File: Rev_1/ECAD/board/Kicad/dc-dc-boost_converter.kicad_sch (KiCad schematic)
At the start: 90 parts, among them Q1 NPN, Q100 IPP029N15NM6, Q101 NPN, Q102 NPN, Q103 PMOS, SW1 SW_DIP_x04, U100 LM3478MA, U2 LM358, U3 LM358, U4 SN74AHC1G02DBVR, U5 SN74AHC1G02DBVR

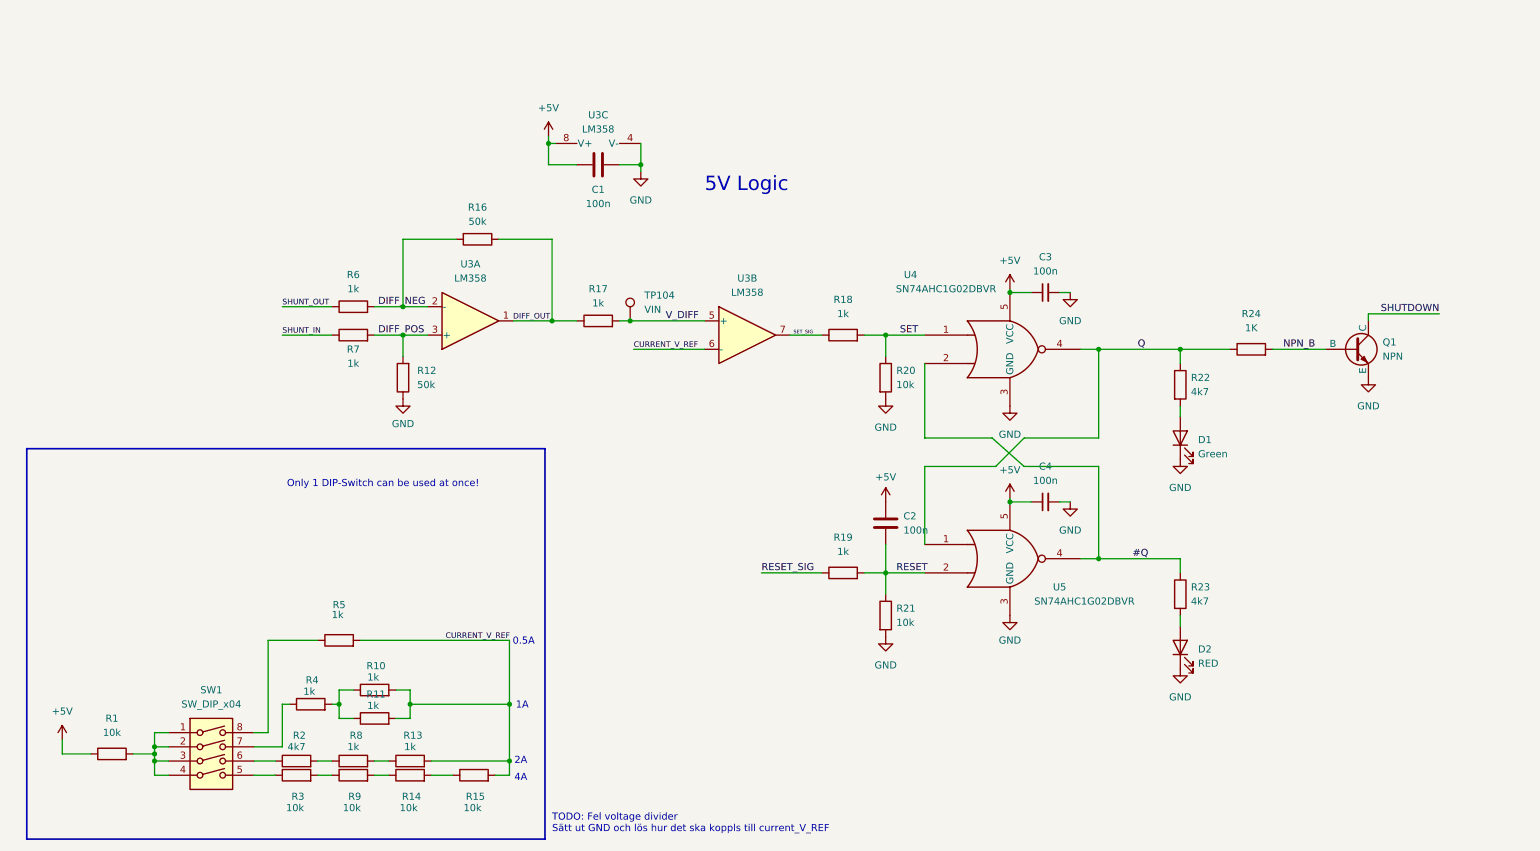
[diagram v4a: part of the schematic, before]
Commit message: -15V schematic is mostly complete
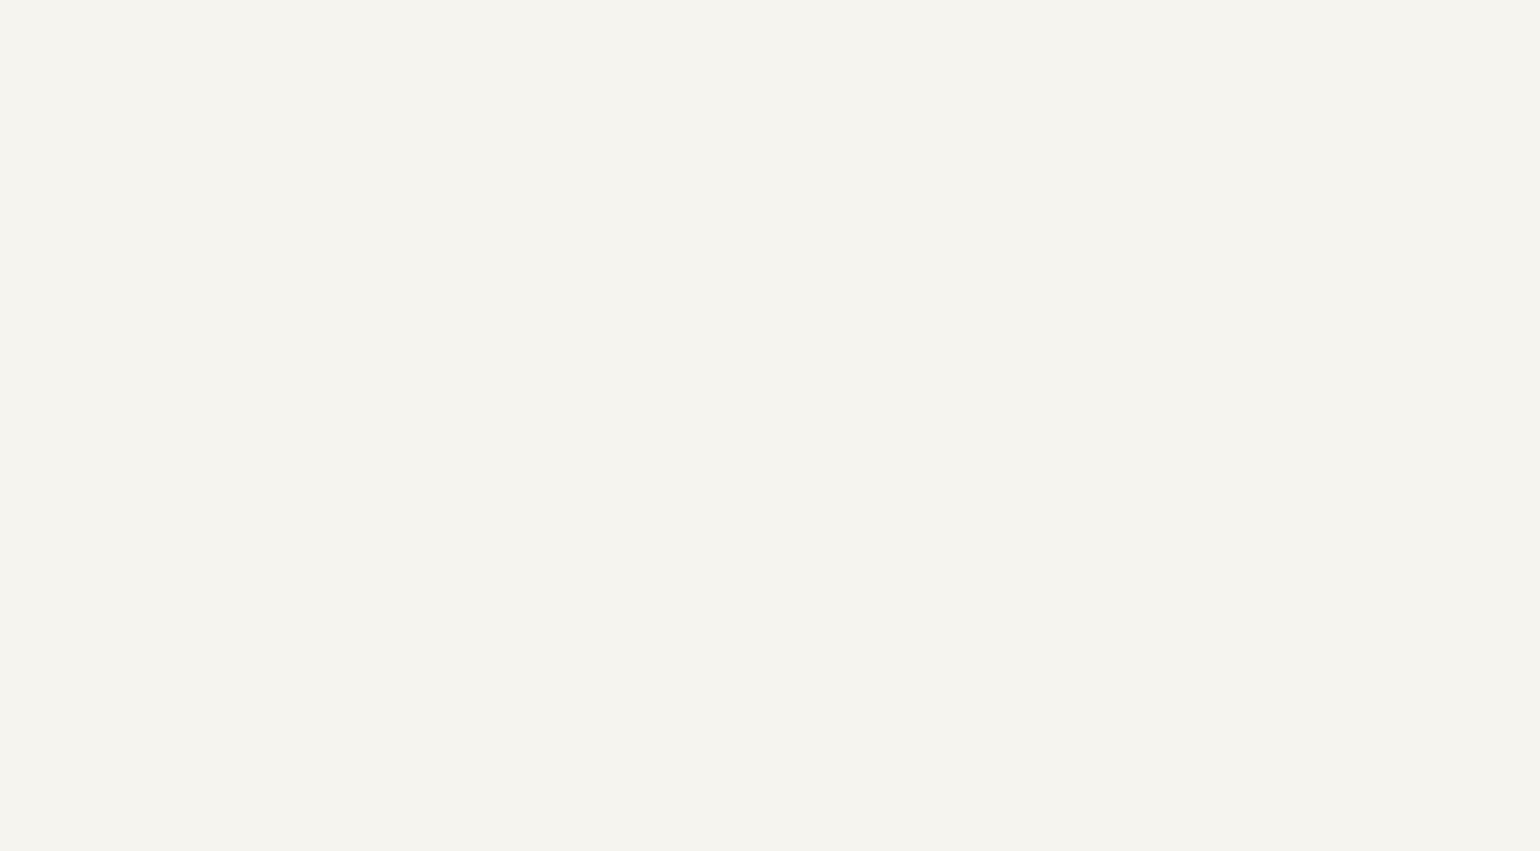
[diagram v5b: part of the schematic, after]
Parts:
- removed C1, C2: 100n, Capacitor_SMD:C_0603_1608Metric_Pad1.08x0.95mm_HandSolder, symbol Device:C
- removed C3, C4: 100n, Capacitor_SMD:C_0603_1608Metric_Pad1.08x0.95mm_HandSolder, symbol Device:C_Small
- removed D1: Green, LED_SMD:LED_0805_2012Metric_Pad1.15x1.40mm_HandSolder, symbol Device:LED
- removed D2: RED, LED_SMD:LED_0805_2012Metric_Pad1.15x1.40mm_HandSolder, symbol Device:LED
- removed Q1: NPN, Package_TO_SOT_SMD:SOT-23_Handsoldering, symbol Simulation_SPICE:NPN
- removed R1, R14, R15, R20, R21, R3, R9: 10k, Resistor_SMD:R_0805_2012Metric_Pad1.20x1.40mm_HandSolder, symbol Device:R
- removed R10, R11, R13, R17, R18, R19, R4, R5, R6, R7, R8: 1k, Resistor_SMD:R_0805_2012Metric_Pad1.20x1.40mm_HandSolder, symbol Device:R
- removed R12, R16: 50k, Resistor_SMD:R_0603_1608Metric_Pad0.98x0.95mm_HandSolder, symbol Device:R
- removed R2, R22, R23: 4k7, Resistor_SMD:R_0805_2012Metric_Pad1.20x1.40mm_HandSolder, symbol Device:R
- removed R24: 1K, Resistor_SMD:R_0805_2012Metric_Pad1.20x1.40mm_HandSolder, symbol Device:R
- removed SW1: SW_DIP_x04, symbol Switch:SW_DIP_x04
- removed TP104: VIN, Connector_Pin:Pin_D0.7mm_L6.5mm_W1.8mm_FlatFork, symbol Connector:TestPoint
- removed U3: LM358, Package_SO:SOIC-8_3.9x4.9mm_P1.27mm, symbol Amplifier_Operational:LM358
- removed U4, U5: SN74AHC1G02DBVR, Package_TO_SOT_SMD:SOT-23-5_HandSoldering, symbol 74xGxx:74AHC1G02
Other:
- note removed: "0.5A"
- note removed: "1A"
- note removed: "2A"
- note removed: "4A"
- note removed: "5V Logic"
- note removed: "Only 1 DIP-Switch can be used at once!"
- note removed: "TODO: Fel voltage divider Sätt ut GND och lös hur det ska koppls till current_V_REF"
